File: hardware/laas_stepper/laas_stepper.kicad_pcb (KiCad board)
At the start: 2 copper layers, 80 x 60 mm, 12 parts, among them J1 Conn_01x04_Pin, J2 Conn_01x04_Pin, J3 Conn_01x04_Pin, J4 Conn_01x02_Pin, U1 Pico

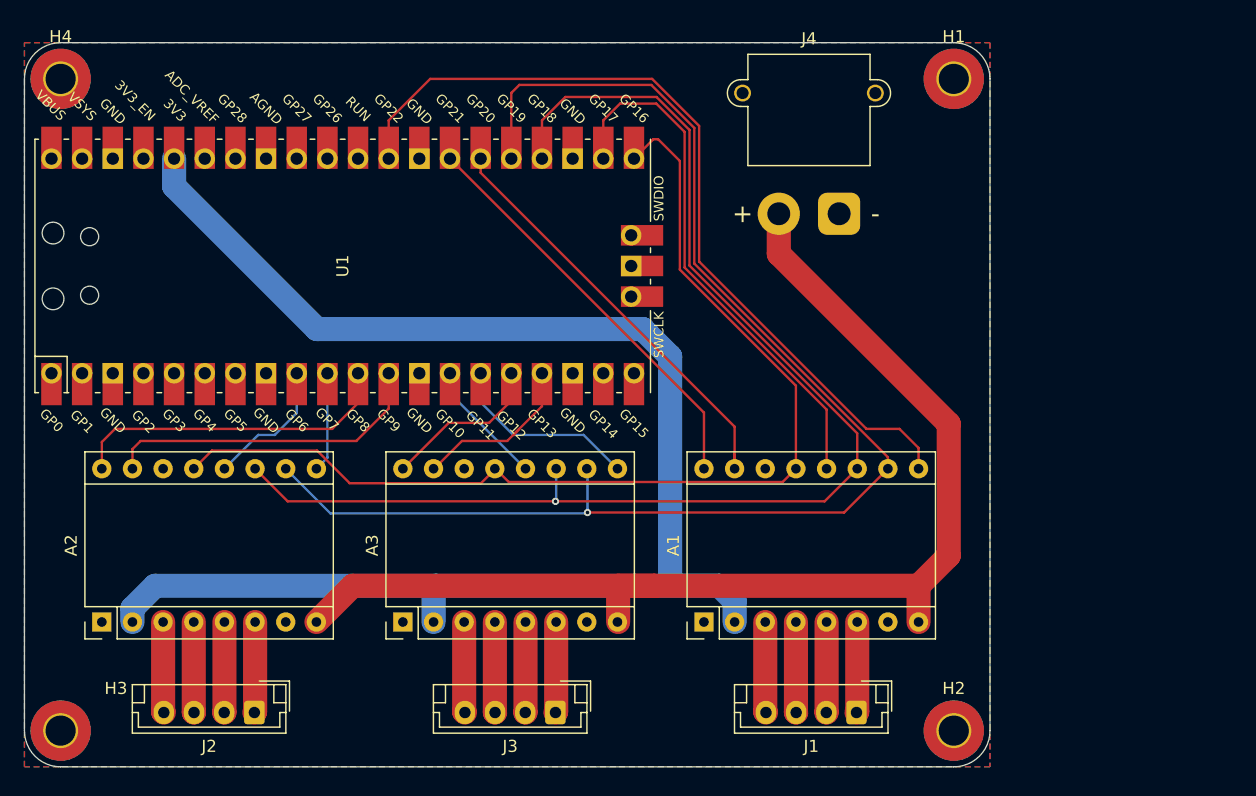
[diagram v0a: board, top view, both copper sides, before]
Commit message: 4 axis version, with UV LED controller + GROVE connector; nex single axis with DC DC to make usb power optional, with GROVE connectors
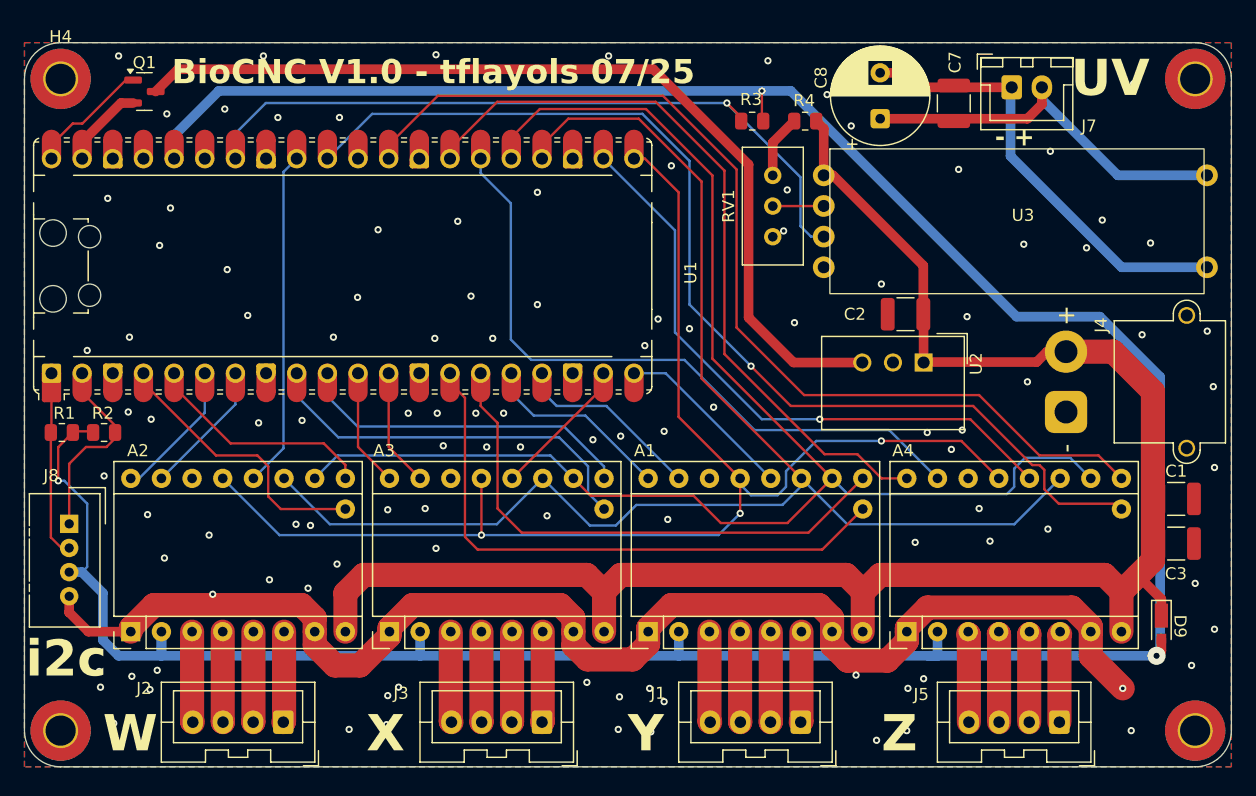
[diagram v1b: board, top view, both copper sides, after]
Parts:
- added A4: SilentStepStick-TMC2130, TMC2301:Pololu_Breakout-16_15.2x20.3mm, F.Cu at (189.1, 158.8)
- added C1: C, Capacitor_SMD:C_1210_3225Metric, F.Cu at (211.4, 147.8)
- added C2: 22u 50V, Capacitor_SMD:C_1210_3225Metric, F.Cu at (189.0, 132.5)
- added C3: C, Capacitor_SMD:C_1210_3225Metric, F.Cu at (211.4, 151.5)
- added C7: C, Capacitor_SMD:C_1210_3225Metric, F.Cu at (193.0, 115.0)
- added C8: C_Polarized, Capacitor_THT:CP_Radial_D8.0mm_P3.80mm, F.Cu at (186.9, 116.3)
- added D9: MSS1P4-M3, Diode_SMD:D_MicroSMP_AK, F.Cu at (210.2, 158.4)
- added J5: Conn_01x04_Pin, Connector_JST:JST_XA_B04B-XASK-1_1x04_P2.50mm_Vertical, F.Cu at (201.8, 166.3)
- added J7: Conn_01x02, Connector_JST:JST_XH_B2B-XH-A_1x02_P2.50mm_Vertical, F.Cu at (197.8, 113.7)
- added J8: Conn_01x04, Connector:NS-Tech_Grove_1x04_P2mm_Vertical, F.Cu at (119.7, 149.9)
- added Q1: DMG2301L, Package_TO_SOT_SMD:SOT-23, F.Cu at (125.9, 114.0)
- added R1: 10k, Resistor_SMD:R_0805_2012Metric, F.Cu at (119.1, 142.3)
- added R2: 10k, Resistor_SMD:R_0805_2012Metric, F.Cu at (122.6, 142.3)
- added R3: 10k, Resistor_SMD:R_0805_2012Metric, F.Cu at (176.3, 116.5)
- added R4: 200k, Resistor_SMD:R_0805_2012Metric, F.Cu at (180.7, 116.5)
- added RV1: 100k, Potentiometer_THT:Potentiometer_Bourns_3296W_Vertical, F.Cu at (178.0, 121.0)
- added U2: TSR1-2433E, Converter_DCDC:Converter_DCDC_TRACO_TSR1-xxxxE_THT, F.Cu at (190.5, 136.5)
- added U3: ~, Library_custom:RCD-24_PL, F.Cu at (198.7, 124.8)
- A1, A2, A3: footprint Module:Pololu_Breakout-16_15.2x20.3mm -> TMC2301:Pololu_Breakout-16_15.2x20.3mm
- J1, J2, J3: footprint Connector_JST:JST_EH_B4B-EH-A_1x04_P2.50mm_Vertical -> Connector_JST:JST_XA_B04B-XASK-1_1x04_P2.50mm_Vertical
- U1: footprint MCU_RaspberryPi_and_Boards:RPi_Pico_SMD_TH -> Module:RaspberryPi_Pico_Common_Unspecified
- moved J4 25.0 mm to (202.3, 140.6), turned to -90 degrees
- moved H1 20.0 mm to (213.0, 113.0)
- moved H2 20.0 mm to (213.0, 167.0)
- moved A1 4.69 mm to (167.7, 158.8)
- moved J1 4.69 mm to (180.3, 166.3)
- moved A2 2.53 mm to (124.8, 158.8)
- moved J2 2.53 mm to (137.4, 166.3)
- moved J3 1.37 mm to (158.9, 166.3)
- moved A3 1.37 mm to (146.2, 158.8)
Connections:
- A1 pad 12: /CS_X -> /CS_Y
- A1 pad 15: /STEP_X -> /STEP_Y
- A1 pad 16: /DIR_X -> /DIR_Y
- A1 pad 9: /ENA_X -> /ENA_Y
- A2 pad 12: /CS_Y -> /CS_W
- A2 pad 15: /STEP_Y -> /STEP_W
- A2 pad 16: /DIR_Y -> /DIR_W
- A2 pad 9: /ENA_Y -> /ENA_W
- A3 pad 12: /CS_Z -> /CS_X
- A3 pad 15: /STEP_Z -> /STEP_X
- A3 pad 16: /DIR_Z -> /DIR_X
- A3 pad 9: /ENA_Z -> /ENA_X
- U1 pad 1: unconnected-(U1-GPIO0-Pad1) -> Net-(J8-Pin_2)
- U1 pad 10: /ENA_Y -> /ENA_X
- U1 pad 11: /DIR_Y -> /DIR_X
- U1 pad 12: /STEP_Y -> /STEP_X
- U1 pad 13: unconnected-(U1-GND-Pad13) -> GND
- U1 pad 14: /CS_Z -> /DIAG0_Y
- U1 pad 15: /ENA_Z -> /ENA_Y
- U1 pad 16: /DIR_Z -> /DIR_Y
- U1 pad 17: /STEP_Z -> /STEP_Y
- U1 pad 18: unconnected-(U1-GND-Pad18) -> GND
- U1 pad 19: unconnected-(U1-GPIO14-Pad19) -> /CS_X
- U1 pad 2: unconnected-(U1-GPIO1-Pad2) -> Net-(J8-Pin_1)
- U1 pad 20: unconnected-(U1-GPIO15-Pad20) -> /CS_Y
- U1 pad 22: /CS_X -> /CS_Z
- U1 pad 23: unconnected-(U1-GND-Pad23) -> GND
- U1 pad 26: /STEP_X -> /STEP_Z
- U1 pad 27: /DIR_X -> /DIR_Z
- U1 pad 28: unconnected-(U1-GND-Pad28) -> GND
- U1 pad 29: /ENA_X -> /ENA_Z
- U1 pad 3: unconnected-(U1-GND-Pad3) -> GND
- U1 pad 31: unconnected-(U1-GPIO26_ADC0-Pad31) -> /DIAG0_Z
- U1 pad 32: unconnected-(U1-GPIO27_ADC1-Pad32) -> /CS_W
- U1 pad 33: unconnected-(U1-AGND-Pad33) -> GND
- U1 pad 34: unconnected-(U1-GPIO28_ADC2-Pad34) -> Net-(U1-GPIO28_ADC2)
- U1 pad 38: unconnected-(U1-GND-Pad38) -> GND
- U1 pad 39: unconnected-(U1-VSYS-Pad39) -> Net-(Q1-S)
- U1 pad 4: unconnected-(U1-GPIO2-Pad4) -> /DIAG0_W
- U1 pad 40: unconnected-(U1-VBUS-Pad40) -> Net-(Q1-G)
- U1 pad 5: unconnected-(U1-GPIO3-Pad5) -> /ENA_W
- U1 pad 6: unconnected-(U1-GPIO4-Pad6) -> /DIR_W
- U1 pad 7: unconnected-(U1-GPIO5-Pad7) -> /STEP_W
- U1 pad 8: unconnected-(U1-GND-Pad8) -> GND
- U1 pad 9: /CS_Y -> /DIAG0_X
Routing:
- net VDD: track 129.4 -> 243.6 mm, vias 0 -> 3
- net GND: track 0.00 -> 112.0 mm, vias 0 -> 106
- net /DIAG0_Z: track 0.00 -> 88.8 mm, vias 0 -> 1
- net Net-(Q1-D): track 0.00 -> 76.8 mm
- net /ENA_Z: track 16.2 -> 84.3 mm
- net Net-(U1-GPIO28_ADC2): track 0.00 -> 60.8 mm, vias 0 -> 1
- net VMOT: track 97.8 -> 147.7 mm
- net /DIAG0_Y: track 0.00 -> 48.1 mm
- net /DIR_Z: track 13.6 -> 61.3 mm
- net /STEP_Z: track 14.5 -> 56.1 mm
- net /ENA_X: track 69.5 -> 28.2 mm
- net /CS_Z: track 10.5 -> 51.2 mm, vias 0 -> 1
- net /ENA_Y: track 5.87 -> 43.9 mm
- net Net-(J7-Pin_1): track 0.00 -> 37.2 mm
- net Net-(J7-Pin_2): track 0.00 -> 32.6 mm
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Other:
- board size 80 x 60 mm -> 100 x 60 mm
- board text added: "- +"
- board text added: "BioCNC V1.0 - tflayols 07/25"
- board text added: "UV"
- board text added: "W"
- board text added: "X"
- board text added: "Y"
- board text added: "Z"
- board text added: "i2c"
